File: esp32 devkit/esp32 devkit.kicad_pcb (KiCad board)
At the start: 2 copper layers, 87.5 x 50.5 mm, 34 parts, among them J1 Conn_01x19, J2 Conn_01x19, Q1 SS8050, Q2 SS8050, SW1 SW_Push, SW2 SW_Push, U1 AMS1117-3.3, U2 ESP32-WROOM-32E(4MB)

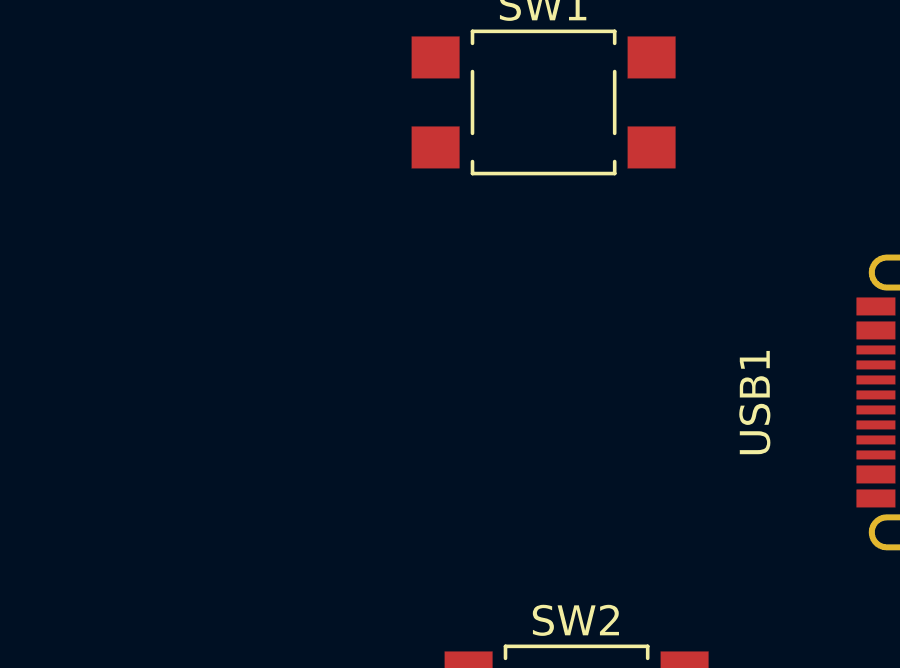
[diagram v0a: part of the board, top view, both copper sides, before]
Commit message: :lipstick::bug:changed LESD5 FOOTPRINT
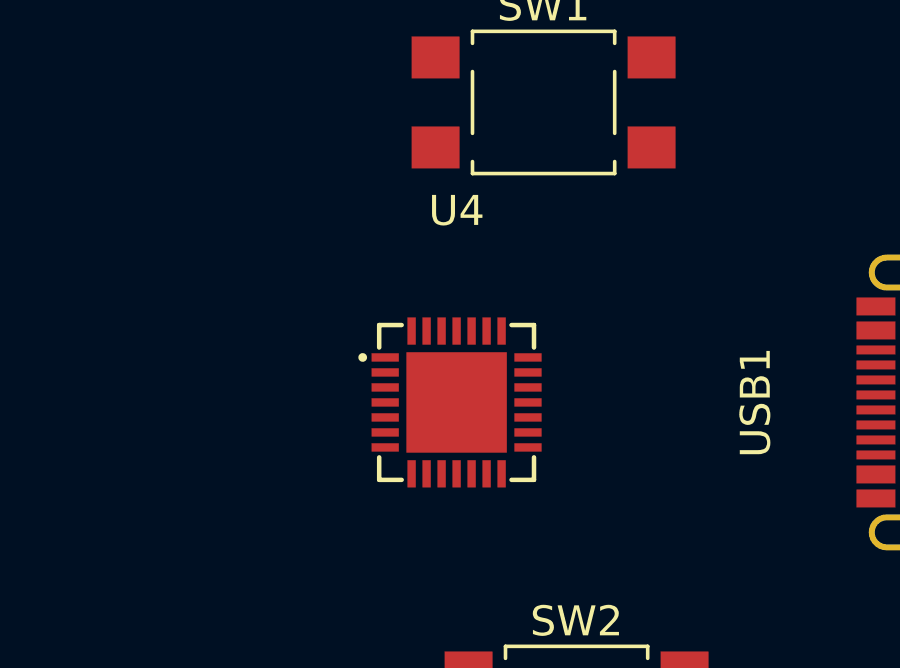
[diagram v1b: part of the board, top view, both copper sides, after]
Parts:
- added U4: CP2102N-A02-GQFN28, CP2102N-A02-GQFN28:QFN-28_L5.0-W5.0-P0.50-TL-EP3.3, F.Cu at (73.5, 132.0)
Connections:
- C9 pad 1: +3.3V -> GND
- C9 pad 2: GND -> +3.3V

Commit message: :memo:Connected LDO AND ESP in editor
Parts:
- added D2: LESD5D5.0CT1G, LESD5D5.0CT1G:TVS_LESD5D5.0CT1G, F.Cu at (87.5, 133.7)
- added D4: LESD5D5.0CT1G, LESD5D5.0CT1G:TVS_LESD5D5.0CT1G, F.Cu at (90.5, 132.0)
- added D5: LESD5D5.0CT1G, LESD5D5.0CT1G:TVS_LESD5D5.0CT1G, F.Cu at (90.3, 133.5)
- J2: moved to B.Cu
- moved C6 338.7 mm to (26.0, 142.0)
- moved R2 333.0 mm to (24.5, 143.5)
- moved C2 317.3 mm to (52.0, 128.5), turned to -90 degrees
- moved C1 315.9 mm to (50.0, 128.2), turned to 90 degrees
- moved C3 312.4 mm to (54.0, 128.0), turned to 90 degrees
- moved D1 310.6 mm to (52.5, 123.5), turned to -90 degrees
- moved R1 307.5 mm to (52.5, 126.0), turned to 90 degrees
- moved C9 307.4 mm to (59.2, 135.0)
- moved C8 304.3 mm to (64.5, 138.5)
- moved C11 303.0 mm to (71.5, 113.0), turned to 90 degrees
- moved R11 302.5 mm to (62.0, 126.5), turned to 180 degrees
- moved Q2 301.6 mm to (64.1, 122.0)
- moved R8 298.5 mm to (64.5, 128.5), turned to -90 degrees
- moved R9 297.7 mm to (65.5, 129.5), turned to -90 degrees
- moved R5 297.4 mm to (61.5, 141.5), turned to 90 degrees
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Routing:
- net +3.3V: track 0.00 -> 27.5 mm
- net /IO13: track 0.00 -> 26.9 mm
- net /IO15: track 0.00 -> 21.3 mm
- net /IO2: track 0.00 -> 18.2 mm
- net /IO4: track 0.00 -> 16.2 mm
- net /IO0: track 0.00 -> 15.8 mm
- net /IO12: track 0.00 -> 15.2 mm
- net /IO14: track 0.00 -> 14.1 mm
- net /IO16: track 0.00 -> 14.0 mm
- net /IO17: track 0.00 -> 13.4 mm
- net /IO5: track 0.00 -> 13.1 mm
- net /1027: track 0.00 -> 13.0 mm
- net /1026: track 0.00 -> 12.5 mm
- net /IO33: track 0.00 -> 12.1 mm
- net /1025: track 0.00 -> 11.9 mm
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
